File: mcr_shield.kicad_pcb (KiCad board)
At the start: 2 copper layers, 110 x 90 mm, 24 parts, among them J2 MCR_P1_Controls, J3 MCR_System_Coin, J4 MCR_Opt_X_Dial, J5 MCR_P2_Controls, SW1 Game_Selector, SW2 Cabinet_Options, U1 Buck_Regulator, U2 Optocoupler_P1, U3 Optocoupler_Sys, U4 Sync_Buffer, U5 Audio_Amplifier

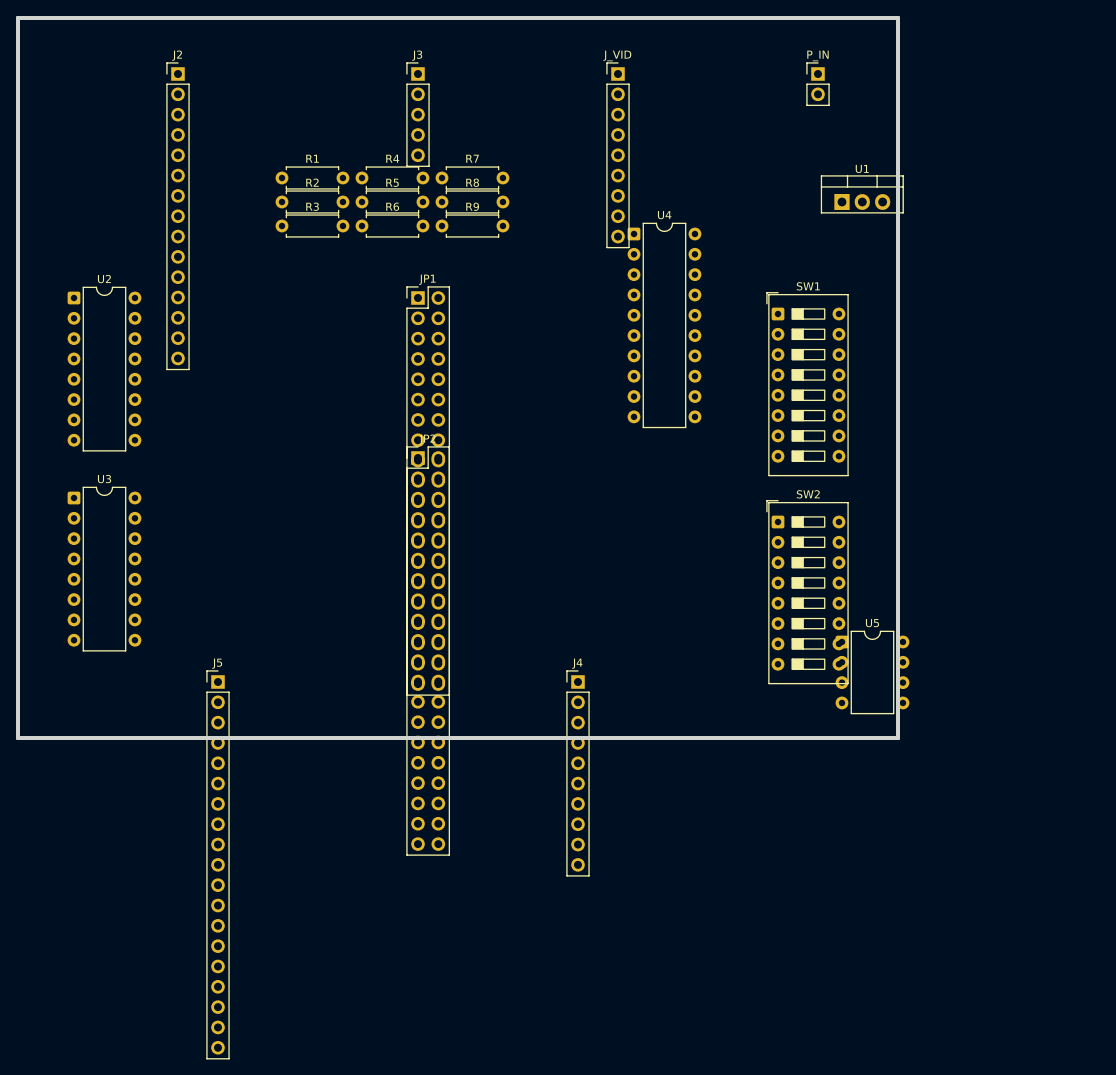
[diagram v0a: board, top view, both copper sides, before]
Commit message: Rotate edge connectors horizontally and draw Tang Console silkscreen keepout outline
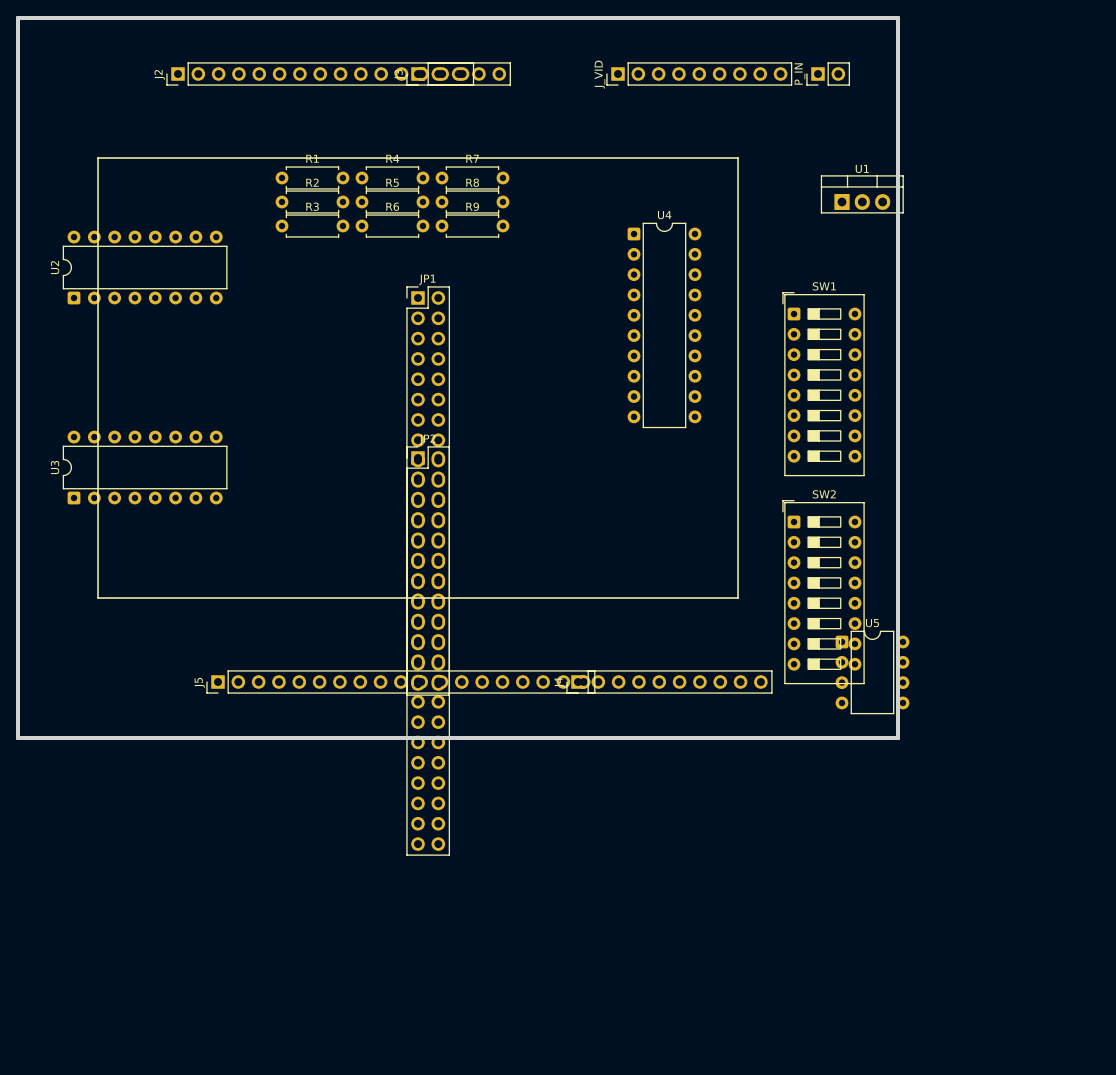
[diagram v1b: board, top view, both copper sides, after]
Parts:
- moved SW1 2.00 mm to (102.0, 42.0)
- moved SW2 2.00 mm to (102.0, 68.0)
- turned J2 to 90 degrees
- turned J3 to 90 degrees
- turned J4 to 90 degrees
- turned J5 to 90 degrees
- turned J_VID to 90 degrees
- turned P_IN to 90 degrees
- turned U2 to 90 degrees
- turned U3 to 90 degrees

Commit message: Incorporate native TangMega138K_Console footprint, expand board to 135x95, and regenerate plots
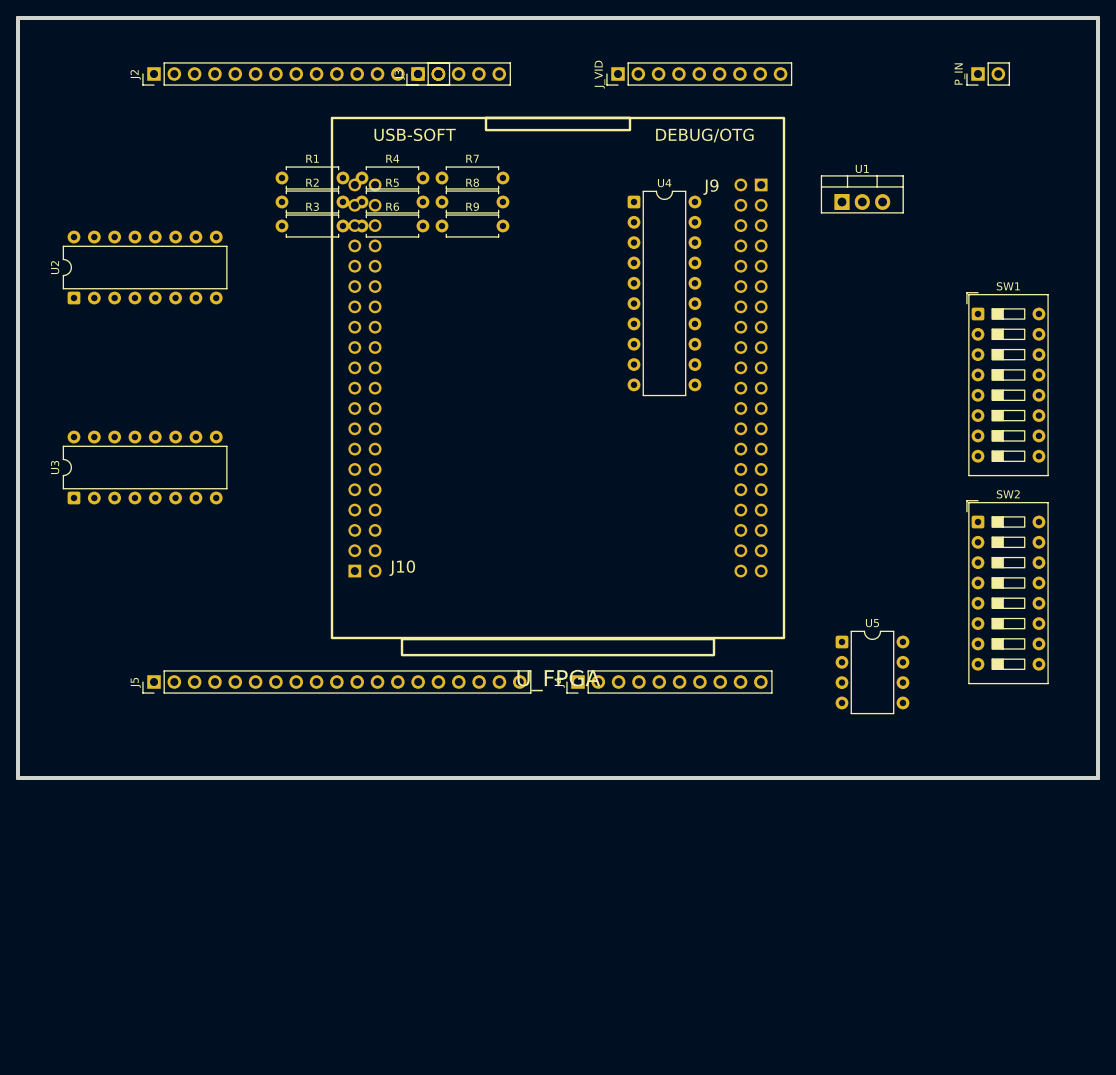
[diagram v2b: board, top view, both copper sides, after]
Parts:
- removed JP1: Tang_2x20_H1, PinHeader_2x20_P2.54mm_Vertical
- removed JP2: Tang_2x20_H2, PinHeader_2x20_P2.54mm_Vertical
- added U_FPGA: TangMega138K_Console, TangMega138K_Console, F.Cu at (72.5, 50.0)
- moved SW1 23.0 mm to (125.0, 42.0)
- moved SW2 23.0 mm to (125.0, 68.0)
- moved P_IN 20.0 mm to (125.0, 12.0)
- moved J5 8.00 mm to (22.0, 88.0)
- moved U4 4.00 mm to (82.0, 28.0)
- moved J2 3.00 mm to (22.0, 12.0)
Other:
- board size 110 x 90 mm -> 135 x 95 mm
